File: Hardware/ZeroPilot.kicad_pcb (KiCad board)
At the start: 2 copper layers, 80 x 100 mm, 197 parts, among them J1 CONN_01X04, J10 PWM, J11 PWM, J12 PWM, J13 PWM, J14 SPOX-2, J15 CONN_02X05, J16 SPOX-3, J17 SPOX-3, J18 SPOX-4, J19 SPOX-2, J2 PWM, J20 SPOX-3, J21 SPOX-3, J22 SPOX-3, J23 SPOX-5, J24 SPOX-5, J25 SPOX-4, J26 SPOX-4, J27 SPOX-4, J28 SPOX-6, J29 SPOX-6, J3 PWM, J30 SPOX-6, J31 SPOX-6, J32 CONN_01X02, J33 SPOX-6, J34 SPOX-6, J35 SPOX-6, J36 SPOX-6, J37 Micro_SD_Card, J4 PWM, J5 PWM, J6 PWM, J7 PWM, J8 PWM, J9 PWM, Q1 Q_PMOS_DGS, U1 NLAS4599, U10 NLAS4599, U11 NLAS4599, U12 NLAS4599, U13 TS30013-M050QFNR, U14 TS30013-M050QFNR, U15 MCP1826S-3302E/DB, U16 STM32F765ZGT6, U17 NC7SZ125P5X, U18 NC7SZ125P5X, U19 STM32F030R8T6, U2 NLAS4599, U20 M24C64-WDW6TP, U3 NLAS4599, U4 NLAS4599, U5 NLAS4599, U6 NLAS4599, U7 NLAS4599, U8 NLAS4599, U9 NLAS4599, Y1 32.768kHz, Y2 8MHz

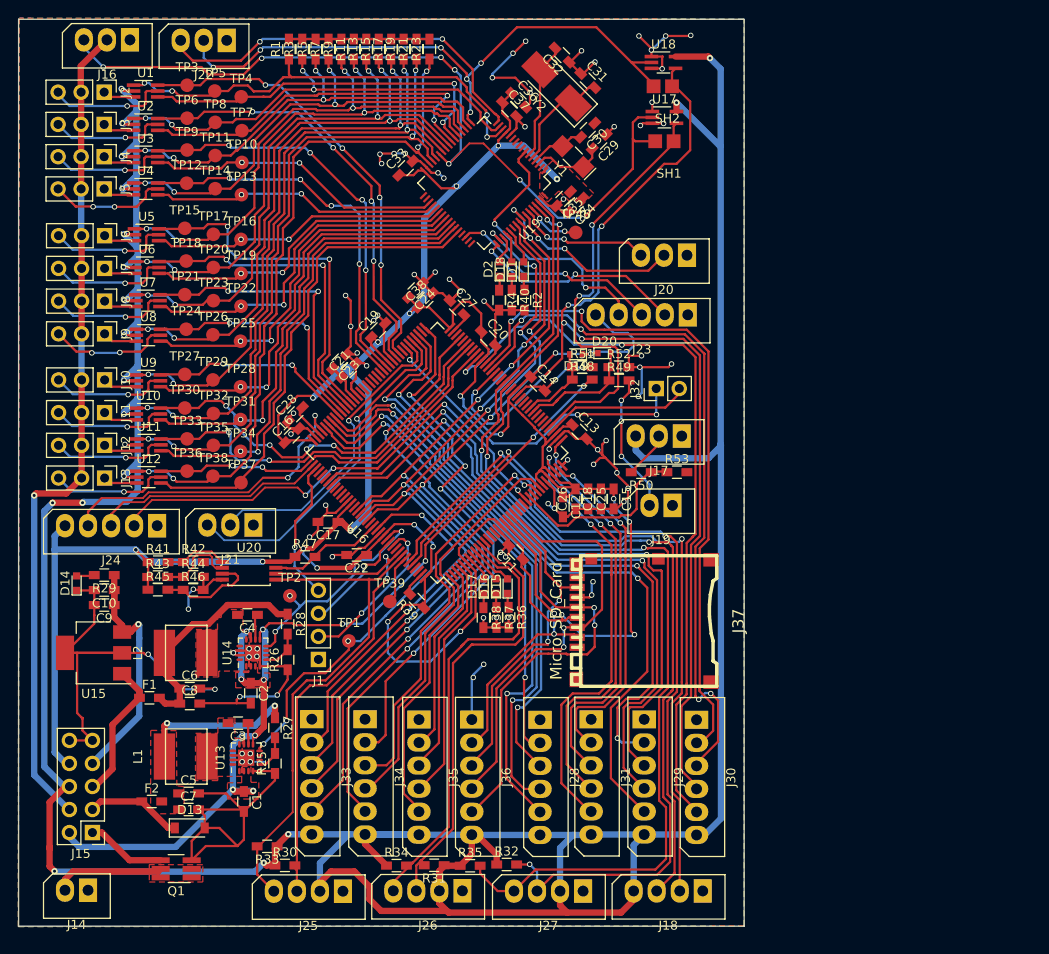
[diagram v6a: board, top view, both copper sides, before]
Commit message: Holy Power
Added a ton of stitching to the power section. Never enough vias.
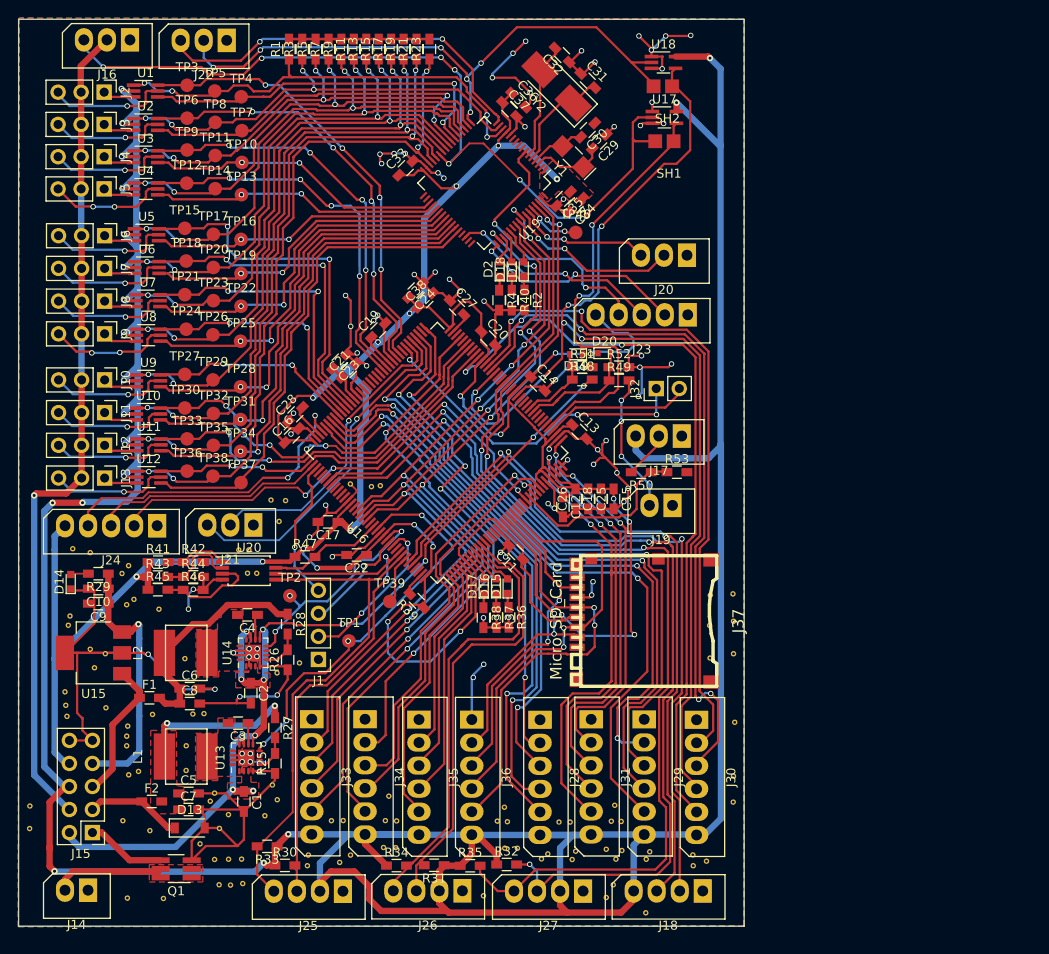
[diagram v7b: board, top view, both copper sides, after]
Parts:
- added REF**: via, WARG:via, F.Cu at (88.9, 101.5)
- added REF**: via, WARG:via, F.Cu at (126.3, 113.5)
- added REF**: via, WARG:via, F.Cu at (66.0, 146.9)
- added REF**: via, WARG:via, F.Cu at (62.0, 146.9)
- added REF**: via, WARG:via, F.Cu at (51.2, 139.2)
- added REF**: via, WARG:via, F.Cu at (51.2, 136.7)
- added REF**: via, WARG:via, F.Cu at (55.2, 125.6)
- added REF**: via, WARG:via, F.Cu at (55.1, 124.2)
- added REF**: via, WARG:via, F.Cu at (55.3, 126.9)
- added REF**: via, WARG:via, F.Cu at (126.2, 116.8)
- added REF**: via, WARG:via, F.Cu at (126.2, 120.4)
- added REF**: via, WARG:via, F.Cu at (128.8, 116.4)
- added REF**: via, WARG:via, F.Cu at (128.8, 120.0)
- added REF**: via, WARG:via, F.Cu at (129.0, 127.5)
- added REF**: via, WARG:via, F.Cu at (128.8, 133.5)
- added REF**: via, WARG:via, F.Cu at (128.8, 136.3)
- added REF**: via, WARG:via, F.Cu at (119.2, 148.5)
- added REF**: via, WARG:via, F.Cu at (125.8, 142.8)
- added REF**: via, WARG:via, F.Cu at (89.9, 101.4)
- added REF**: via, WARG:via, F.Cu at (124.4, 143.3)
- added REF**: via, WARG:via, F.Cu at (124.3, 142.1)
- added REF**: via, WARG:via, F.Cu at (101.3, 146.6)
- added REF**: via, WARG:via, F.Cu at (114.8, 146.8)
- added REF**: via, WARG:via, F.Cu at (115.6, 145.4)
- added REF**: via, WARG:via, F.Cu at (90.8, 135.7)
- added REF**: via, WARG:via, F.Cu at (91.6, 141.3)
- added REF**: via, WARG:via, F.Cu at (90.2, 141.3)
- added REF**: via, WARG:via, F.Cu at (91.7, 138.4)
- added REF**: via, WARG:via, F.Cu at (90.4, 138.4)
- added REF**: via, WARG:via, F.Cu at (86.6, 101.2)
- added REF**: via, WARG:via, F.Cu at (85.8, 138.3)
- added REF**: via, WARG:via, F.Cu at (84.5, 138.4)
- added REF**: via, WARG:via, F.Cu at (105.0, 141.4)
- added REF**: via, WARG:via, F.Cu at (103.6, 141.4)
- added REF**: via, WARG:via, F.Cu at (103.9, 138.5)
- added REF**: via, WARG:via, F.Cu at (102.8, 138.4)
- added REF**: via, WARG:via, F.Cu at (110.8, 138.5)
- added REF**: via, WARG:via, F.Cu at (109.6, 138.5)
- added REF**: via, WARG:via, F.Cu at (116.4, 138.5)
- added REF**: via, WARG:via, F.Cu at (115.4, 138.4)
- added REF**: via, WARG:via, F.Cu at (78.7, 105.4)
- added REF**: via, WARG:via, F.Cu at (114.8, 141.5)
- added REF**: via, WARG:via, F.Cu at (119.6, 141.8)
- added REF**: via, WARG:via, F.Cu at (119.2, 142.6)
- added REF**: via, WARG:via, F.Cu at (116.5, 141.7)
- added REF**: via, WARG:via, F.Cu at (115.9, 142.6)
- added REF**: via, WARG:via, F.Cu at (111.0, 142.6)
- added REF**: via, WARG:via, F.Cu at (111.4, 141.7)
- added REF**: via, WARG:via, F.Cu at (107.7, 142.6)
- added REF**: via, WARG:via, F.Cu at (108.4, 142.0)
- added REF**: via, WARG:via, F.Cu at (86.6, 142.2)
- added REF**: via, WARG:via, F.Cu at (79.4, 103.1)
- added REF**: via, WARG:via, F.Cu at (85.4, 143.0)
- added REF**: via, WARG:via, F.Cu at (81.8, 143.3)
- added REF**: via, WARG:via, F.Cu at (81.9, 142.2)
- added REF**: via, WARG:via, F.Cu at (78.5, 122.1)
- added REF**: via, WARG:via, F.Cu at (81.0, 121.0)
- added REF**: via, WARG:via, F.Cu at (57.9, 108.8)
- added REF**: via, WARG:via, F.Cu at (56.0, 108.4)
- added REF**: via, WARG:via, F.Cu at (75.4, 108.5)
- added REF**: via, WARG:via, F.Cu at (74.3, 108.5)
- added REF**: via, WARG:via, F.Cu at (76.3, 111.1)
- added REF**: via, WARG:via, F.Cu at (77.8, 103.0)
- added REF**: via, WARG:via, F.Cu at (75.2, 111.1)
- added REF**: via, WARG:via, F.Cu at (69.3, 111.5)
- added REF**: via, WARG:via, F.Cu at (62.1, 110.2)
- added REF**: via, WARG:via, F.Cu at (61.4, 111.1)
- added REF**: via, WARG:via, F.Cu at (61.9, 114.6)
- added REF**: via, WARG:via, F.Cu at (65.5, 115.0)
- added REF**: via, WARG:via, F.Cu at (62.7, 114.0)
- added REF**: via, WARG:via, F.Cu at (55.5, 116.8)
- added REF**: via, WARG:via, F.Cu at (55.7, 115.8)
- added REF**: via, WARG:via, F.Cu at (57.9, 119.5)
- added REF**: via, WARG:via, F.Cu at (103.6, 136.9)
- added REF**: via, WARG:via, F.Cu at (58.4, 121.5)
- added REF**: via, WARG:via, F.Cu at (59.6, 120.0)
- added REF**: via, WARG:via, F.Cu at (68.3, 120.5)
- added REF**: via, WARG:via, F.Cu at (70.4, 126.6)
- added REF**: via, WARG:via, F.Cu at (69.2, 126.6)
- added REF**: via, WARG:via, F.Cu at (78.0, 134.4)
- added REF**: via, WARG:via, F.Cu at (78.5, 136.1)
- added REF**: via, WARG:via, F.Cu at (77.2, 137.8)
- added REF**: via, WARG:via, F.Cu at (74.6, 142.6)
- added REF**: via, WARG:via, F.Cu at (73.2, 142.6)
- added REF**: via, WARG:via, F.Cu at (115.7, 136.7)
- added REF**: via, WARG:via, F.Cu at (71.6, 142.6)
- added REF**: via, WARG:via, F.Cu at (74.7, 145.3)
- added REF**: via, WARG:via, F.Cu at (72.1, 145.4)
- added REF**: via, WARG:via, F.Cu at (73.4, 145.5)
- added REF**: via, WARG:via, F.Cu at (61.5, 138.4)
- added REF**: via, WARG:via, F.Cu at (64.5, 139.5)
- added REF**: via, WARG:via, F.Cu at (62.0, 127.9)
- added REF**: via, WARG:via, F.Cu at (64.8, 126.6)
- added REF**: via, WARG:via, F.Cu at (59.6, 125.9)
- added REF**: via, WARG:via, F.Cu at (61.9, 129.0)
- added REF**: via, WARG:via, F.Cu at (128.8, 113.4)
- added REF**: via, WARG:via, F.Cu at (61.9, 130.1)
- added REF**: via, WARG:via, F.Cu at (63.2, 132.9)
- added REF**: via, WARG:via, F.Cu at (62.1, 133.3)
- added REF**: via, WARG:via, F.Cu at (68.5, 130.1)
- added REF**: via, WARG:via, F.Cu at (68.5, 132.8)
- added REF**: via, WARG:via, F.Cu at (71.1, 136.2)
- added REF**: via, WARG:via, F.Cu at (71.6, 135.3)
- added REF**: via, WARG:via, F.Cu at (73.1, 137.7)
- added REF**: via, WARG:via, F.Cu at (72.1, 139.2)
- added REF**: via, WARG:via, F.Cu at (70.0, 140.9)
- moved C9 0.67 mm to (58.8, 114.4)
- moved C10 0.67 mm to (58.8, 112.8)
- moved D14 0.67 mm to (55.7, 112.0)
- moved R29 0.67 mm to (58.8, 111.1)
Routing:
- net /5V_INT: track 418.8 -> 426.5 mm
- net /3V3: track 374.3 -> 377.4 mm
- net /POWER/3V3_JMP: track 28.5 -> 31.1 mm
- net GND: track 384.0 -> 386.5 mm

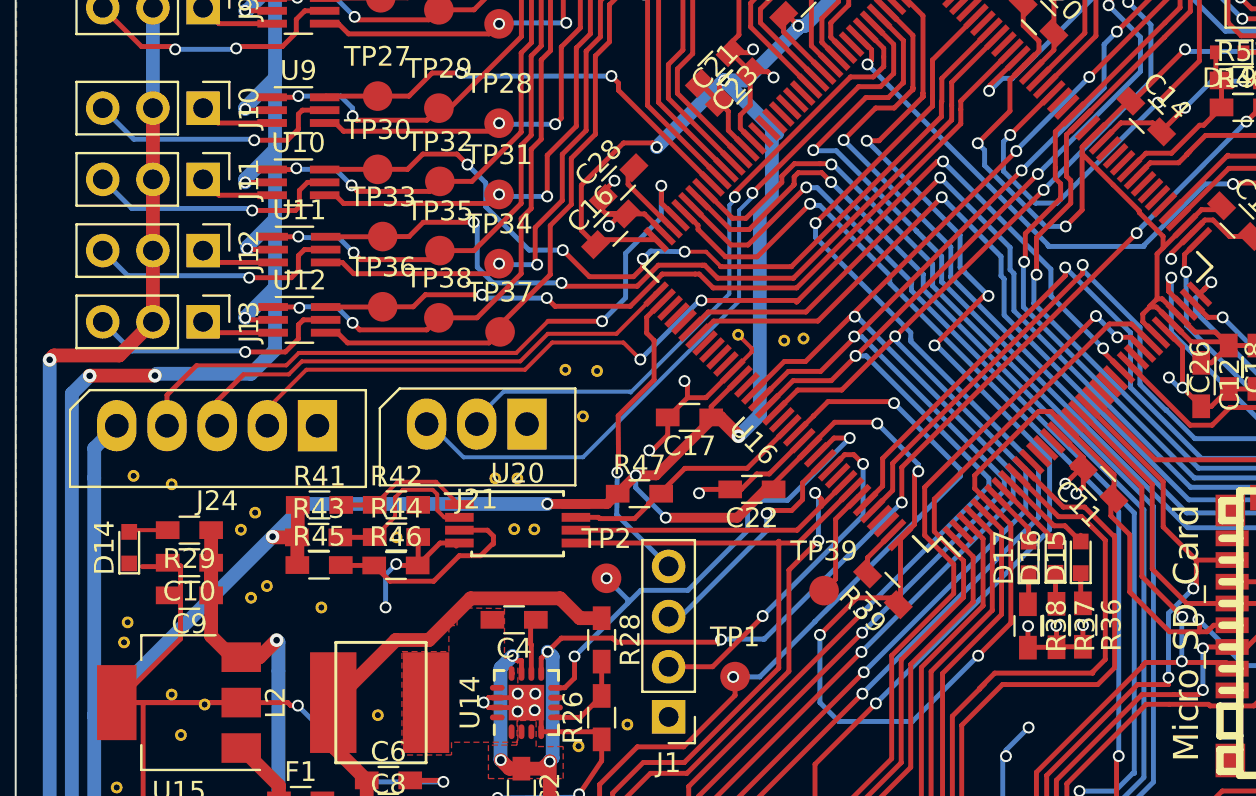
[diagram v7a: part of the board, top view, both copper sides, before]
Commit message: Holy Pilot
Added stiching around STMF7 chip
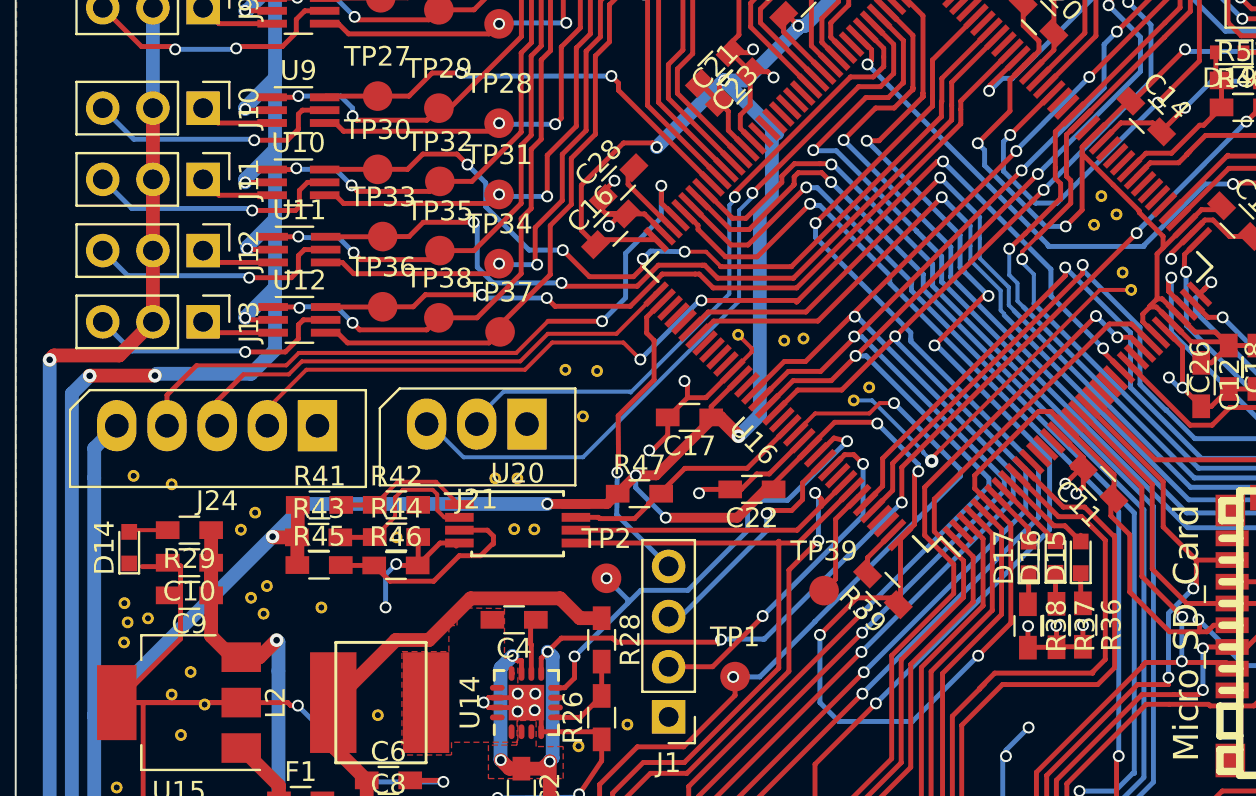
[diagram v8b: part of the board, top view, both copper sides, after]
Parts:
- added REF**: via, WARG:via, F.Cu at (106.5, 99.0)
- added REF**: via, WARG:via, F.Cu at (55.5, 114.8)
- added REF**: via, WARG:via, F.Cu at (56.7, 115.6)
- added REF**: via, WARG:via, F.Cu at (106.0, 98.1)
- added REF**: via, WARG:via, F.Cu at (105.7, 95.1)
- added REF**: via, WARG:via, F.Cu at (105.0, 94.2)
- added REF**: via, WARG:via, F.Cu at (104.6, 95.7)
- added REF**: via, WARG:via, F.Cu at (92.4, 104.6)
- added REF**: via, WARG:via, F.Cu at (93.2, 103.9)
- added REF**: via, WARG:via, F.Cu at (62.6, 115.4)
- added REF**: via, WARG:via, F.Cu at (58.9, 118.3)
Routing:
- net GND: track 386.5 -> 405.6 mm, vias 79 -> 80
- net /SCL4: track 115.3 -> 116.0 mm
- net /SDA4: track 116.8 -> 117.5 mm
